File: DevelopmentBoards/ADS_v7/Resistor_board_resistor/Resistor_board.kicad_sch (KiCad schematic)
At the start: 6 parts, among them J1 Conn_01x06_Pin, SW1 SW_SPDT_312

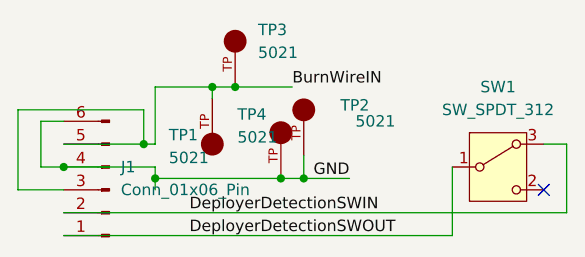
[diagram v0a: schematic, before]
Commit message: ADS v7: Corrected layout of converter, replaced tp pads with thp pads in resistor board, some other minor trace layout changes
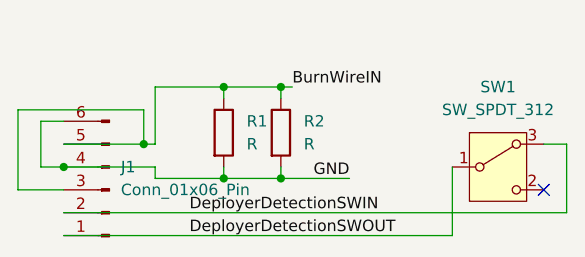
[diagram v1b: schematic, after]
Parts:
- removed TP1, TP2, TP3, TP4: 5021, 5021:TP_5021, symbol 5021:5021
- added R1, R2: R, Resistor_THT:R_Axial_DIN0207_L6.3mm_D2.5mm_P7.62mm_Horizontal, symbol Device:R
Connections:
- net BurnWireIN: now also R1.1, R2.1
- net GND: now also R1.2, R2.2
